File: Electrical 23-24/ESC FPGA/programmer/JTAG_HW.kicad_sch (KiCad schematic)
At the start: 44 parts, among them J1 USB_B_Micro, J2 SFH11-PBPC-D07-ST-BK, J3 Conn_01x05_Pin, J4 Conn_01x11_Pin, J5 Conn_01x14_Pin, SW1 SW_DPST, U1 93CxxC, U2 AMS1117-3.3, U3 NUP2202, U4 FT2232HL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

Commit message: idk but something
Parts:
- added R14: 0, symbol Device:R
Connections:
- net +3.3V: now also R14.2; no longer J2.2
- new net: J2.2, R14.1
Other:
- moved on the sheet: C13, C14, C15, C7, J2

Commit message: DR Feedback
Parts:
- added C8: 3.3uF, Capacitor_SMD:C_0805_2012Metric_Pad1.18x1.45mm_HandSolder, symbol Device:C_Small
- FB1, FB2: value FerriteBead_Small -> BLM18KG121TN1D; Digi (none) -> https://www.digikey.com/en/products/detail/murata-electroni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
- U1: value 93CxxC -> 93C46C
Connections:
- net +1V8: now also C8.1
- net GND: now also C8.2
- net at U4.7 (DM): now also J1.2 (D-), U3.1; no longer R7.2
- net at U4.8 (DP): now also J1.3 (D+), U3.6; no longer R6.2
- now unconnected: R6.1, R7.1
- no-connect marks 11 -> 15
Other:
- note added: "add short clip"
- note added: "check r"
- note added: "check these pins"
- note added: "make sure caps are correct drop in replacement?"
- note added: "resistors needed?"
- note added: "this seems unnecessary"
- moved on the sheet: C10, C11, C12, C13, C14, C15, C2, C3, C6, C7, C9, D1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

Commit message: Update JTAG_HW.kicad_sch
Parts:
- removed R6, R7: 27, Resistor_SMD:R_0805_2012Metric_Pad1.20x1.40mm_HandSolder, symbol Device:R_Small
- J4: symbol Connector:Conn_01x11_Pin -> Connector:Conn_01x13_Pin
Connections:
- net SUS: now reaches U4.36 (~{SUSPEND})
- net SUS: now also J4.13 (Pin_13)
- net PWREN: now reaches U4.60 (~{PWREN})
- net PWREN: now also J4.12 (Pin_12)
- no-connect marks 15 -> 9
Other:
- note removed: "add short clip"
- note removed: "check r"
- note removed: "check these pins"
- note removed: "resistors needed?"
- note removed: "this seems unnecessary"

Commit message: Finish programmer schematic w/ Digi
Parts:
- removed C5: 27pF, Capacitor_SMD:C_0805_2012Metric_Pad1.18x1.45mm_HandSolder, symbol Device:C_Small
- removed Y1: 12MHZ, Crystal:Crystal_SMD_0603-2Pin_6.0x3.5mm_HandSoldering, symbol Device:Crystal
- added X1: ISM92-3351AH-12.000MHZ, Oscillator:Oscillator_SMD_Abracon_ASE-4Pin_3.2x2.5mm_HandSoldering, symbol Oscillator:ASE-xxxMHz
- C1, C11, C12, C13, C14, C15, C2, C3, C6, C7, C8, C9: footprint Capacitor_SMD:C_0805_2012Metric_Pad1.18x1.45mm_HandSolder -> Capacitor_SMD:C_0603_1608Metric_Pad1.08x0.95mm_HandSolder
- C10: footprint Capacitor_Tantalum_SMD:CP_EIA-3216-18_Kemet-A_Pad1.58x1.35mm_HandSolder -> Capacitor_SMD:C_0603_1608Metric_Pad1.08x0.95mm_HandSolder
- C4: value 27pF -> 0.01uF; footprint Capacitor_SMD:C_0805_2012Metric_Pad1.18x1.45mm_HandSolder -> Capacitor_SMD:C_0603_1608Metric_Pad1.08x0.95mm_HandSolder
- D1, D2, D3: footprint LED_SMD:LED_0805_2012Metric_Pad1.15x1.40mm_HandSolder -> LED_SMD:LED_0603_1608Metric_Pad1.05x0.95mm_HandSolder
- D4: footprint (none) -> Diode_SMD:D_0603_1608Metric_Pad1.05x0.95mm_HandSolder; Digi (none) -> https://www.digikey.com/en/products/detail/kyocera-avx/SD06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
- FB1, FB2: footprint Inductor_SMD:L_0805_2012Metric_Pad1.15x1.40mm_HandSolder -> Inductor_SMD:L_0603_1608Metric_Pad1.05x0.95mm_HandSolder
- J2: Digi (none) -> https://www.digikey.com/en/products/detail/sullins-connecto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; Pair (none) -> https://www.digikey.com/en/products/detail/sullins-connecto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
- J4: value Conn_01x11_Pin -> Conn_01x13_Pin; footprint Connector_PinHeader_2.54mm:PinHeader_1x11_P2.54mm_Vertical -> Connector_PinHeader_2.54mm:PinHeader_1x13_P2.54mm_Vertical
- R1, R10, R11, R2, R3, R4, R5, R8, R9: footprint Resistor_SMD:R_0805_2012Metric_Pad1.20x1.40mm_HandSolder -> Resistor_SMD:R_0603_1608Metric_Pad0.98x0.95mm_HandSolder
- R12, R13, R14: footprint (none) -> Resistor_SMD:R_0603_1608Metric_Pad0.98x0.95mm_HandSolder
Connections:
- net +3.3V: now also C4.2, X1.1 (EN), X1.4 (Vdd)
- net GND: now also C4.1, X1.2 (GND); no longer C4.2
- net at U4.2 (OSCI): now also X1.3 (OUT); no longer C4.1
- no-connect marks 9 -> 10
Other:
- note removed: "make sure caps are correct drop in replacement?"
- moved on the sheet: C4

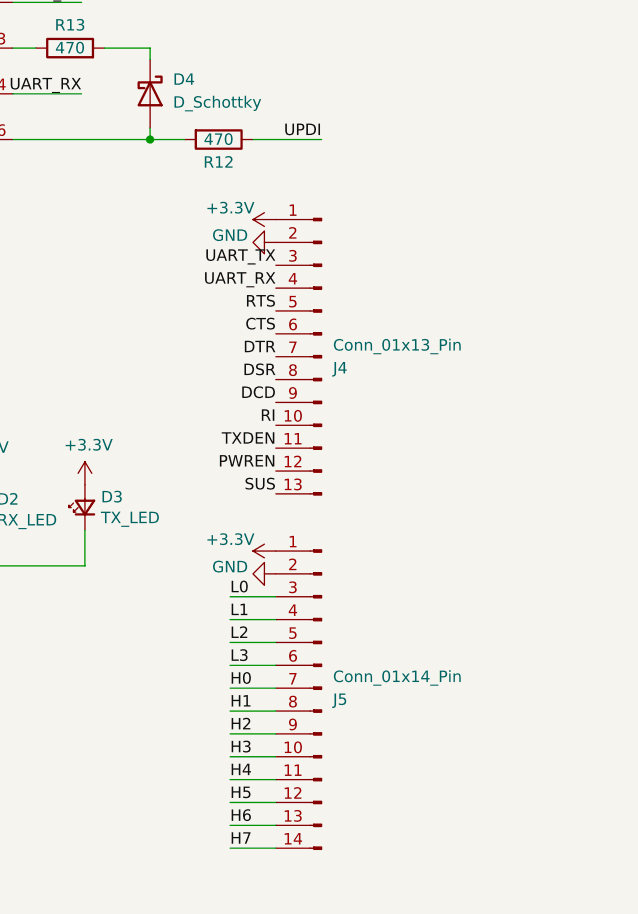
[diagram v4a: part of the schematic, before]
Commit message: Layout almost done, need to try routing
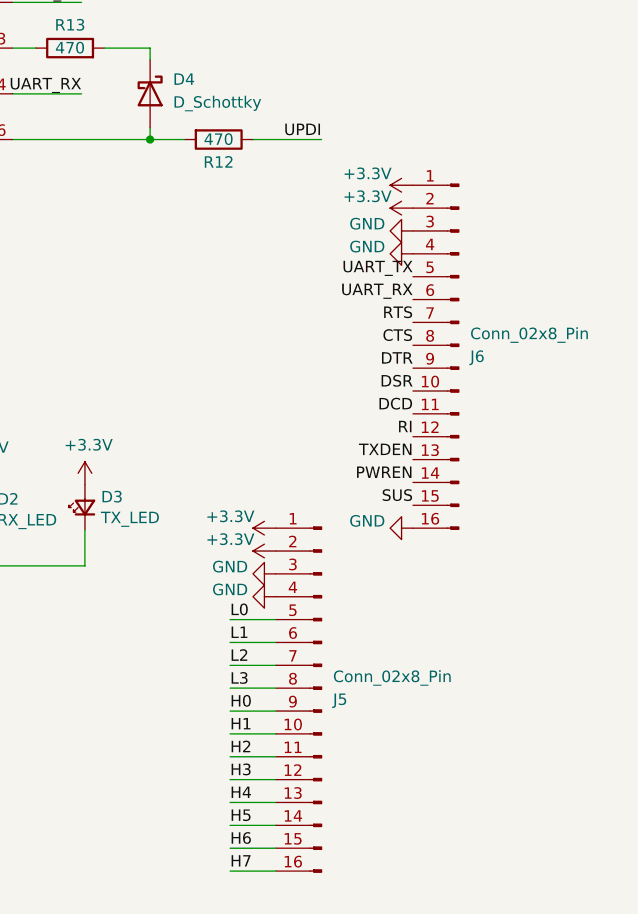
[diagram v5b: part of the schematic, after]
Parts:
- removed J4: Conn_01x13_Pin, Connector_PinHeader_2.54mm:PinHeader_1x13_P2.54mm_Vertical, symbol Connector:Conn_01x13_Pin
- added J6: Conn_02x8_Pin, Connector_PinHeader_2.54mm:PinHeader_2x08_P2.54mm_Vertical, symbol Connector:Conn_01x16_Pin
- J3: footprint Connector_PinHeader_2.54mm:PinHeader_1x05_P2.54mm_Vertical -> Connector_PinSocket_2.54mm:PinSocket_1x05_P2.54mm_Horizontal
- J5: value Conn_01x14_Pin -> Conn_02x8_Pin; footprint Connector_PinHeader_2.54mm:PinHeader_1x14_P2.54mm_Vertical -> Connector_PinHeader_2.54mm:PinHeader_2x08_P2.54mm_Vertical; symbol Connector:Conn_01x14_Pin -> Connector:Conn_01x16_Pin
- U2: footprint Package_TO_SOT_SMD:SOT-223-3_TabPin2 -> Package_TO_SOT_SMD:SOT-223
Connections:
- net +3.3V: now also J5.2 (Pin_2), J6.1 (Pin_1), J6.2 (Pin_2)
- net CTS: now also J6.8 (Pin_8)
- net DCD: now also J6.11 (Pin_11)
- net DSR: now also J6.10 (Pin_10)
- net DTR: now also J6.9 (Pin_9)
- net GND: now also J5.3 (Pin_3), J5.4 (Pin_4), J6.16 (Pin_16), J6.3 (Pin_3), J6.4 (Pin_4); no longer J5.2 (Pin_2)
- net H0: now also J5.9 (Pin_9); no longer J5.7 (Pin_7)
- net H1: now also J5.10 (Pin_10); no longer J5.8 (Pin_8)
- net H2: now also J5.11 (Pin_11); no longer J5.9 (Pin_9)
- net H3: now also J5.12 (Pin_12); no longer J5.10 (Pin_10)
- net H4: now also J5.13 (Pin_13); no longer J5.11 (Pin_11)
- net H5: now also J5.14 (Pin_14); no longer J5.12 (Pin_12)
- net H6: now also J5.15 (Pin_15); no longer J5.13 (Pin_13)
- net H7: now also J5.16 (Pin_16); no longer J5.14 (Pin_14)
- net L0: now also J5.5 (Pin_5); no longer J5.3 (Pin_3)
- net L1: now also J5.6 (Pin_6); no longer J5.4 (Pin_4)
- net L2: now also J5.7 (Pin_7); no longer J5.5 (Pin_5)
- net L3: now also J5.8 (Pin_8); no longer J5.6 (Pin_6)
- net PWREN: now also J6.14 (Pin_14)
- net RI: now also J6.12 (Pin_12)
- net RTS: now also J6.7 (Pin_7)
- net SUS: now also J6.15 (Pin_15)
- net TXDEN: now also J6.13 (Pin_13)
- net UART_RX: now also J6.6 (Pin_6)
- net UART_TX: now also J6.5 (Pin_5)

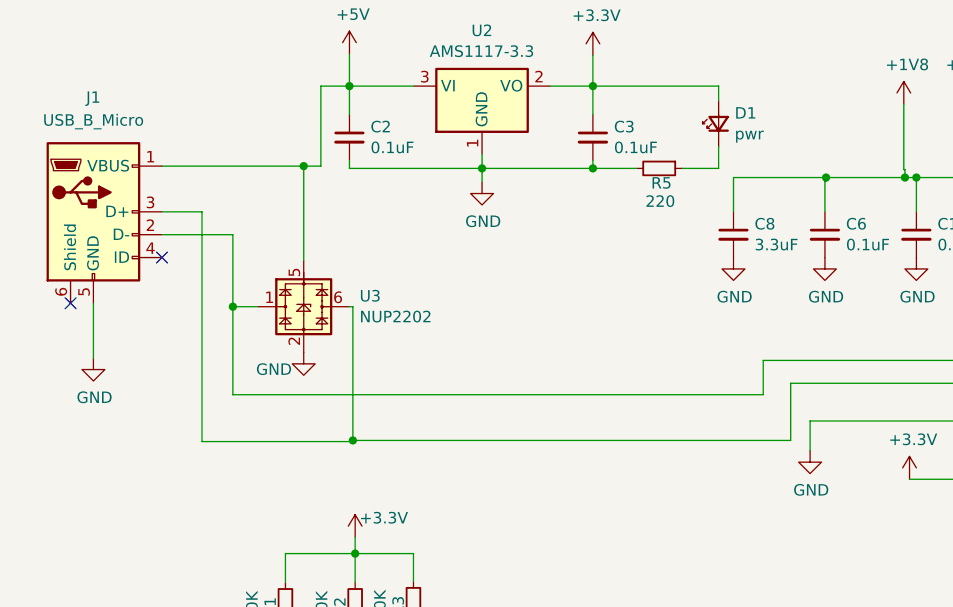
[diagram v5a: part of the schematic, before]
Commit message: Finished the core, connecting ports
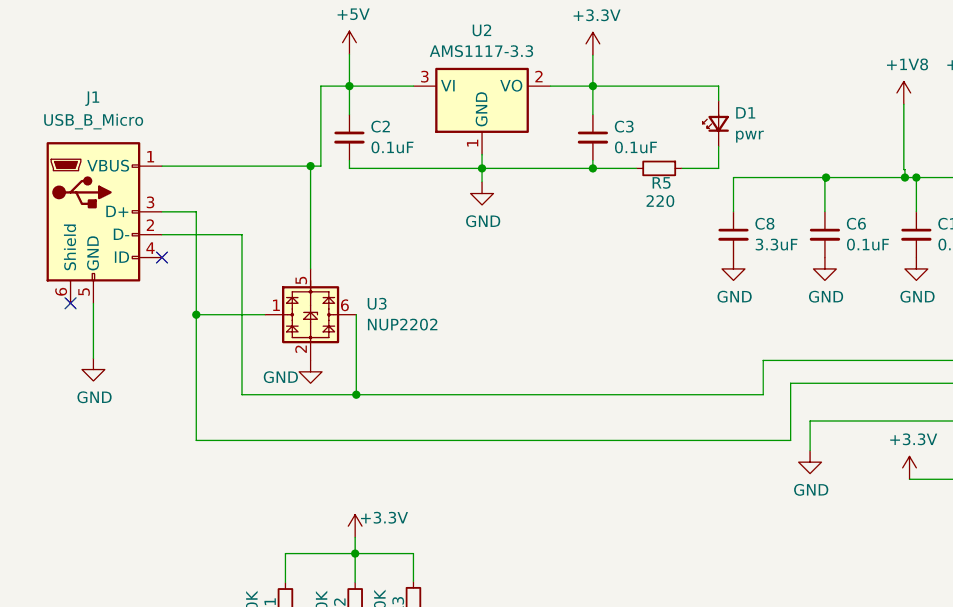
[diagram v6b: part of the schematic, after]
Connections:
- net at J1.2 (D-), U4.7 (DM): now also U3.6; no longer U3.1
- net at J1.3 (D+), U4.8 (DP): now also U3.1; no longer U3.6
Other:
- moved on the sheet: U3
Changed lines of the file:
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@@
   (junction (at 64.643 120.523) (diameter 0) (color 0 0 0 0)
   )
-  (junction (at 64.389 90.17) (diameter 0) (color 0 0 0 0)
-  )
   (junction (at 30.226 129.921) (diameter 0) (color 0 0 0 0)
   )
@@
   (junction (at 233.68 36.83) (diameter 0) (color 0 0 0 0)
   )
+  (junction (at 64.77 85.09) (diameter 0) (color 0 0 0 0)
+  )
   (junction (at 71.12 122.936) (diameter 0) (color 0 0 0 0)
   )
@@
   (junction (at 162.56 161.925) (diameter 0) (color 0 0 0 0)
   )
+  (junction (at 59.69 59.69) (diameter 0) (color 0 0 0 0)
+  )
   (junction (at 245.11 86.36) (diameter 0) (color 0 0 0 0)
   )
@@
   (junction (at 233.68 29.21) (diameter 0) (color 0 0 0 0)
   )
-  (junction (at 51.054 75.311) (diameter 0) (color 0 0 0 0)
-  )
-  (junction (at 58.928 59.69) (diameter 0) (color 0 0 0 0)
+  (junction (at 46.99 76.2) (diameter 0) (color 0 0 0 0)
   )
   (no_connect (at 203.2 127))
@@
     (stroke (width 0) (type default))
   )
-  (wire (pts (xy 53.848 75.311) (xy 51.054 75.311))
-    (stroke (width 0) (type default))
-  )
   (wire (pts (xy 26.797 116.078) (xy 26.797 127.381))
     (stroke (width 0) (type default))
@@
     (stroke (width 0) (type default))
   )
+  (wire (pts (xy 43.18 59.69) (xy 59.69 59.69))
+    (stroke (width 0) (type default))
+  )
   (wire (pts (xy 157.48 161.925) (xy 157.734 161.925))
     (stroke (width 0) (type default))
   )
-  (wire (pts (xy 58.928 70.231) (xy 58.928 59.69))
+  (wire (pts (xy 59.69 71.12) (xy 59.69 59.69))
     (stroke (width 0) (type default))
   )
@@
     (stroke (width 0) (type default))
   )
+  (wire (pts (xy 46.99 76.2) (xy 54.61 76.2))
+    (stroke (width 0) (type default))
+  )
   (wire (pts (xy 56.515 129.921) (xy 74.676 129.921))
     (stroke (width 0) (type default))
@@
     (stroke (width 0) (type default))
   )
-  (wire (pts (xy 64.389 90.17) (xy 113.03 90.17))
+  (wire (pts (xy 46.99 90.17) (xy 113.03 90.17))
     (stroke (width 0) (type default))
   )
@@
     (stroke (width 0) (type default))
   )
-  (wire (pts (xy 47.625 64.77) (xy 47.625 90.297))
+  (wire (pts (xy 46.99 76.2) (xy 46.99 90.17))
     (stroke (width 0) (type default))
   )
@@
     (stroke (width 0) (type default))
   )
-  (wire (pts (xy 43.18 67.31) (xy 51.054 67.31))
+  (wire (pts (xy 43.18 67.31) (xy 52.07 67.31))
     (stroke (width 0) (type default))
   )
@@
     (stroke (width 0) (type default))
   )
+  (wire (pts (xy 64.77 85.09) (xy 109.982 85.09))
+    (stroke (width 0) (type default))
+  )
   (wire (pts (xy 172.72 48.26) (xy 172.72 44.45))
     (stroke (width 0) (type default))
@@
     (stroke (width 0) (type default))
   )
-  (wire (pts (xy 60.833 59.69) (xy 58.928 59.69))
+  (wire (pts (xy 60.833 59.69) (xy 59.69 59.69))
     (stroke (width 0) (type default))
   )
@@
     (stroke (width 0) (type default))
   )
-  (wire (pts (xy 51.054 75.311) (xy 51.054 85.09))
+  (wire (pts (xy 52.07 67.31) (xy 52.07 85.09))
     (stroke (width 0) (type default))
   )
@@
     (stroke (width 0) (type default))
   )
-  (wire (pts (xy 43.18 59.69) (xy 58.928 59.69))
-    (stroke (width 0) (type default))
-  )
   (wire (pts (xy 237.49 81.28) (xy 229.87 81.28))
     (stroke (width 0) (type default))
@@
     (stroke (width 0) (type default))
   )
-  (wire (pts (xy 51.054 67.31) (xy 51.054 75.311))
-    (stroke (width 0) (type default))
-  )
   (wire (pts (xy 254 160.02) (xy 259.08 160.02))
     (stroke (width 0) (type default))
@@
     (stroke (width 0) (type default))
   )
-  (wire (pts (xy 64.389 75.311) (xy 64.389 90.17))
-    (stroke (width 0) (type default))
-  )
   (wire (pts (xy 233.68 43.18) (xy 233.68 41.91))
     (stroke (width 0) (type default))
@@
     (stroke (width 0) (type default))
   )
-  (wire (pts (xy 47.625 90.297) (xy 64.389 90.297))
-    (stroke (width 0) (type default))
-  )
   (wire (pts (xy 229.87 86.36) (xy 245.11 86.36))
     (stroke (width 0) (type default))
@@
     (stroke (width 0) (type default))
   )
-  (wire (pts (xy 64.389 90.17) (xy 64.389 90.297))
-    (stroke (width 0) (type default))
-  )
   (wire (pts (xy 64.643 102.743) (xy 71.12 102.743))
     (stroke (width 0) (type default))
@@
     (stroke (width 0) (type default))
   )
-  (wire (pts (xy 51.054 85.09) (xy 109.982 85.09))
+  (wire (pts (xy 52.07 85.09) (xy 64.77 85.09))
     (stroke (width 0) (type default))
   )
@@
     (stroke (width 0) (type default))
   )
-  (wire (pts (xy 47.625 64.77) (xy 43.18 64.77))
-    (stroke (width 0) (type default))
-  )
   (wire (pts (xy 233.68 39.37) (xy 233.68 41.91))
     (stroke (width 0) (type default))
@@
     (stroke (width 0) (type default))
   )
+  (wire (pts (xy 64.77 76.2) (xy 64.77 85.09))
+    (stroke (width 0) (type default))
+  )
   (wire (pts (xy 213.36 55.88) (xy 213.36 54.991))
     (stroke (width 0) (type default))
@@
     (stroke (width 0) (type default))
   )
+  (wire (pts (xy 46.99 76.2) (xy 46.99 64.77))
+    (stroke (width 0) (type default))
+  )
   (wire (pts (xy 170.434 43.053) (xy 170.434 44.45))
     (stroke (width 0) (type default))
@@
     (stroke (width 0) (type default))
   )
+  (wire (pts (xy 46.99 64.77) (xy 43.18 64.77))
+    (stroke (width 0) (type default))
+  )
   (wire (pts (xy 233.68 36.83) (xy 233.68 39.37))
-    (stroke (width 0) (type default))
-  )
-  (wire (pts (xy 64.008 75.311) (xy 64.389 75.311))
     (stroke (width 0) (type default))
   )
@@
     )
   )
-  (symbol (lib_id "Power_Protection:NUP2202") (at 58.928 75.311 0) (unit 1)
-    (in_bom yes) (on_board yes) (dnp no)
-    (property "Reference" "U3" (at 65.1256 74.1426 0)
+  (symbol (lib_id "Power_Protection:NUP2202") (at 59.69 76.2 0) (unit 1)
+    (in_bom yes) (on_board yes) (dnp no)
+    (property "Reference" "U3" (at 65.8876 75.0316 0)
       (effects (font (size 1.27 1.27)) (justify left))
     )
-    (property "Value" "NUP2202" (at 65.1256 76.454 0)
+    (property "Value" "NUP2202" (at 65.8876 77.343 0)
       (effects (font (size 1.27 1.27)) (justify left))
     )
-    (property "Footprint" "Package_TO_SOT_SMD:SOT-363_SC-70-6" (at 60.96 73.406 0)
-      (effects (font (size 1.27 1.27)) hide)
-    )
-    (property "Datasheet" "http://www.onsemi.ru.com/pub_link/Collateral/NUP2202W1-D.PDF" (at 60.96 73.406 0)
+    (property "Footprint" "Package_TO_SOT_SMD:SOT-363_SC-70-6" (at 61.722 74.295 0)
+      (effects (font (size 1.27 1.27)) hide)
+    )
+    (property "Datasheet" "http://www.onsemi.ru.com/pub_link/Collateral/NUP2202W1-D.PDF" (at 61.722 74.295 0)
       (effects (font (size 1.27 1.27)) hide)
     )
@@
     )
   )
-  (symbol (lib_id "power:GND") (at 58.928 80.391 0) (unit 1)
-    (in_bom yes) (on_board yes) (dnp no)
-    (property "Reference" "#PWR01" (at 58.928 86.741 0)
-      (effects (font (size 1.27 1.27)) hide)
-    )
-    (property "Value" "GND" (at 55.626 82.296 0)
-      (effects (font (size 1.27 1.27)))
-    )
-    (property "Footprint" "" (at 58.928 80.391 0)
-      (effects (font (size 1.27 1.27)) hide)
-    )
-    (property "Datasheet" "" (at 58.928 80.391 0)
-      (effects (font (size 1.27 1.27)) hide)
-    )
+  (symbol (lib_id "power:GND") (at 59.69 81.28 0) (unit 1)
+    (in_bom yes) (on_board yes) (dnp no)
+    (property "Reference" "#PWR01" (at 59.69 87.63 0)
+      (effects (font (size 1.27 1.27)) hide)
+    )
+    (property "Value" "GND" (at 56.388 83.185 0)
+      (effects (font (size 1.27 1.27)))
+    )
+    (property "Footprint" "" (at 59.69 81.28 0)
+      (effects (font (size 1.27 1.27)) hide)
+    )
+    (property "Datasheet" "" (at 59.69 81.28 0)
+      (effects (font (size 1.27 1.27)) hide)
+    )

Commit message: Finish programmer BOM
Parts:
- U3: Digi (none) -> https://www.digikey.com/en/products/detail/onsemi/NUP2202W1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
- U4: Digi (none) -> https://www.digikey.com/en/products/detail/ftdi-future-tech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
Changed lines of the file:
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@@
+      (effects (font (size 1.27 1.27)) hide)
+    )
+    (property "Digi" "https://www.digikey.com/en/products/detail/ftdi-future-technology-devices-international-ltd/FT2232HL-REEL/1986053" (at 172.72 104.14 0)
       (effects (font (size 1.27 1.27)) hide)
     )
@@
       (effects (font (size 1.27 1.27)) hide)
     )
+    (property "Digi" "https://www.digikey.com/en/products/detail/onsemi/NUP2202W1T2G/1485002?s=N4IgTCBcDaIHIFUAKYwAYIF0C%2BQ" (at 59.69 76.2 0)
+      (effects (font (size 1.27 1.27)) hide)
+    )
